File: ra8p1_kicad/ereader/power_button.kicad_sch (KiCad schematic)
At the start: 37 parts, among them Q1 DMN2056U-7, Q2 DMN2056U-7, SW1 POWER, U10 LM66100DCKR, U11 TPS3808G01DBVR, U12 74LVC1G14GW,125, U9 LTC2954ITS8-1

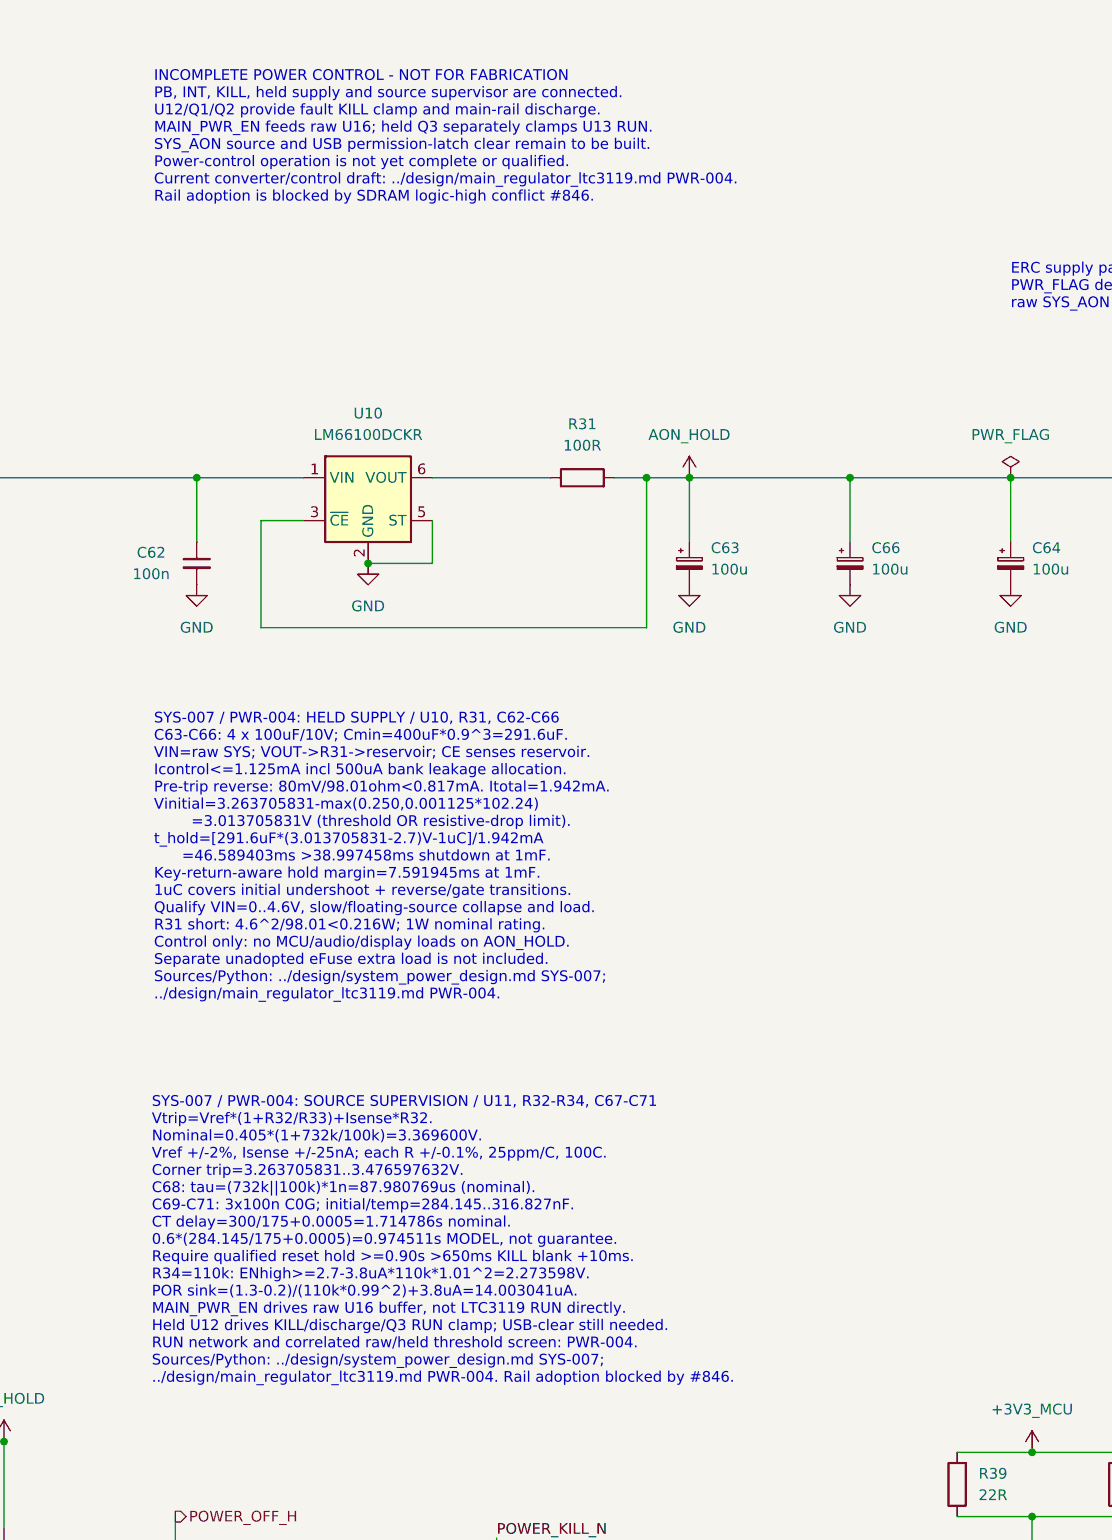
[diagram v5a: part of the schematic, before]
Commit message: Complete MCU reset checkpoint and portable engineering records
Refs #825, #826, #846. Preserve the unresolved radio release margin and unfinished schematic status; refresh full PDF and native BOM.
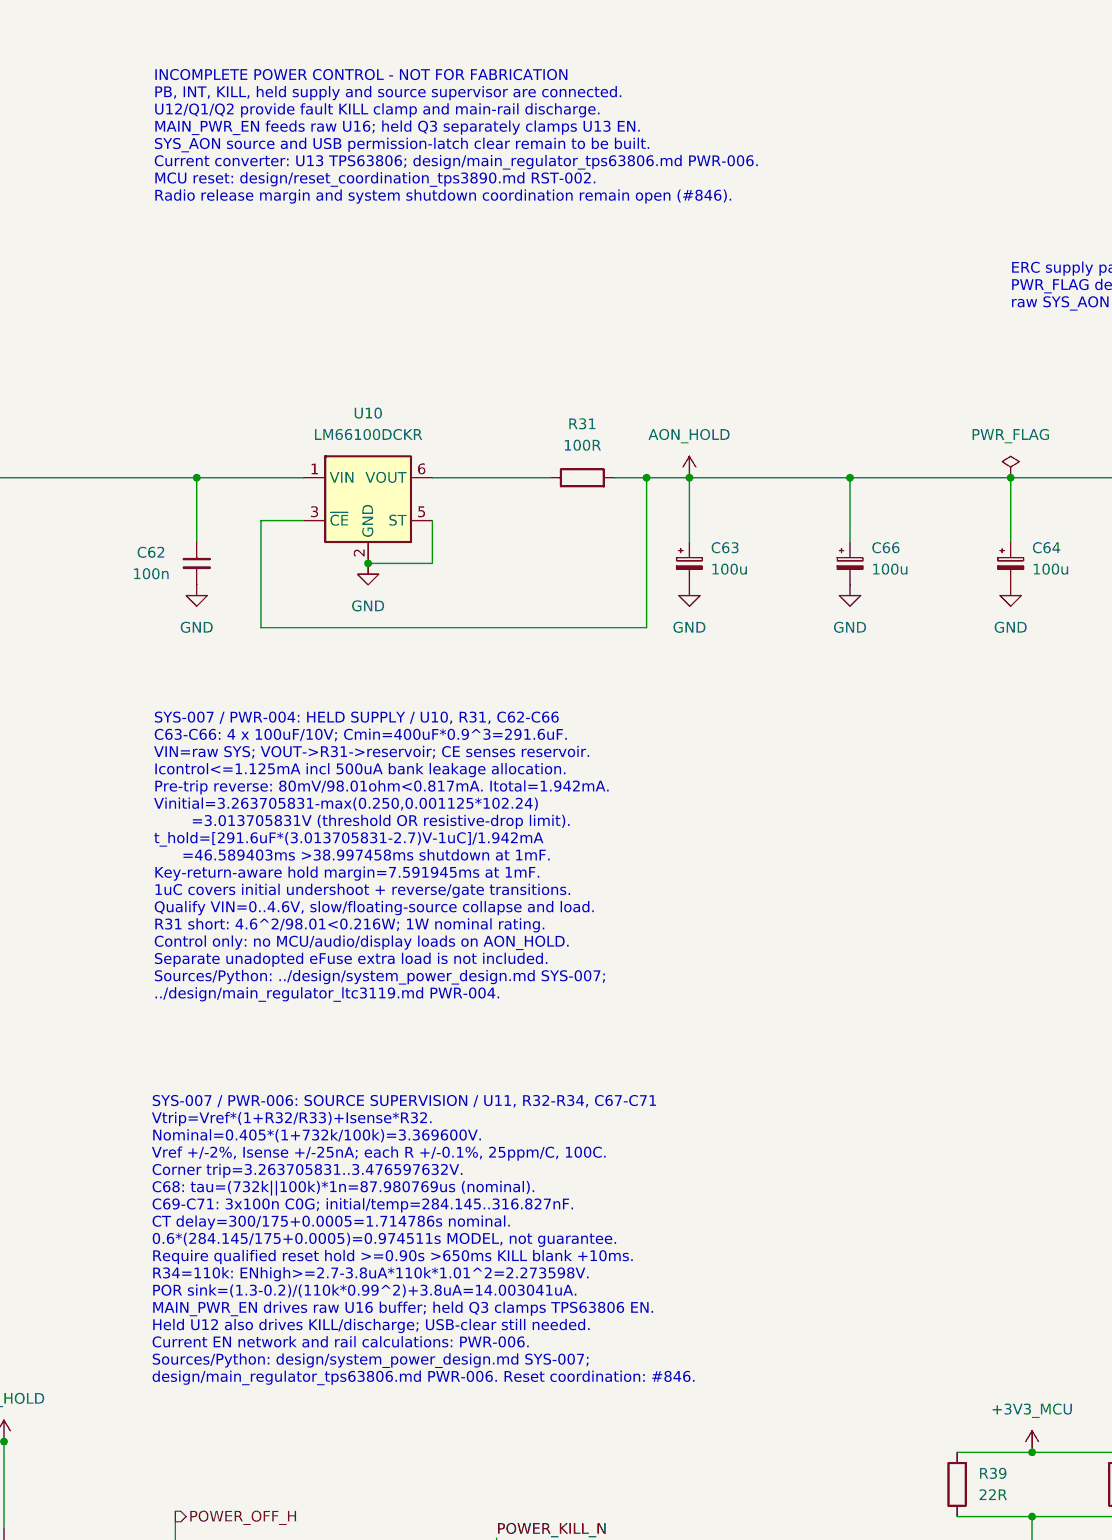
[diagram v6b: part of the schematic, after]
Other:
- note added: "INCOMPLETE POWER CONTROL - NOT FOR FABRICATION PB, INT, KILL, held supply and source supervisor are connected. U12/Q1/Q2 provide fault KILL clamp and main-rail discharge. MAIN_PWR_EN feeds raw U16; held Q3 separately clamps U13 EN. SYS_AON source and USB permission-latch clear remain to be built. Current converter: U13 TPS63806; design/main_regulator_tps63806.md PWR-006. MCU reset: design/reset_c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"
- note added: "SYS-007 / PWR-006: SOURCE SUPERVISION / U11, R32-R34, C67-C71 Vtrip=Vref*(1+R32/R33)+Isense*R32. Nominal=0.405*(1+732k/100k)=3.369600V. Vref +/-2%, Isense +/-25nA; each R +/-0.1%, 25ppm/C, 100C. Corner trip=3.263705831..3.476597632V. C68: tau=(732k||100k)*1n=87.980769us (nominal). C69-C71: 3x100n C0G; initial/temp=284.145..316.827nF. CT delay=300/175+0.0005=1.714786s nominal. 0.6*(284.145/175+0.0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"
- note removed: "INCOMPLETE POWER CONTROL - NOT FOR FABRICATION PB, INT, KILL, held supply and source supervisor are connected. U12/Q1/Q2 provide fault KILL clamp and main-rail discharge. MAIN_PWR_EN feeds raw U16; held Q3 separately clamps U13 RUN. SYS_AON source and USB permission-latch clear remain to be built. Power-control operation is not yet complete or qualified. Current converter/control draft: ../design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"
- note removed: "SYS-007 / PWR-004: SOURCE SUPERVISION / U11, R32-R34, C67-C71 Vtrip=Vref*(1+R32/R33)+Isense*R32. Nominal=0.405*(1+732k/100k)=3.369600V. Vref +/-2%, Isense +/-25nA; each R +/-0.1%, 25ppm/C, 100C. Corner trip=3.263705831..3.476597632V. C68: tau=(732k||100k)*1n=87.980769us (nominal). C69-C71: 3x100n C0G; initial/temp=284.145..316.827nF. CT delay=300/175+0.0005=1.714786s nominal. 0.6*(284.145/175+0.0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"
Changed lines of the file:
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@@
 		(rev "0.3 DRAFT")
 	)
-	(text "SYS-007 / PWR-004: SOURCE SUPERVISION / U11, R32-R34, C67-C71\nVtrip=Vref*(1+R32/R33)+Isense*R32.\nNominal=0.405*(1+732k/100k)=3.369600V.\nVref +/-2%, Isense +/-25nA; each R +/-0.1%, 25ppm/C, 100C.\nCorner trip=3.263705831..3.476597632V.\nC68: tau=(732k||100k)*1n=87.980769us (nominal).\nC69-C71: 3x100n C0G; initial/temp=284.145..316.827nF.\nCT delay=300/175+0.0005=1.714786s nominal.\n0.6*(284.145/175+0.0005)=0.974511s MODEL, not guarantee.\nRequire qualified reset hold >=0.90s >650ms KILL blank +10ms.\nR34=110k: ENhigh>=2.7-3.8uA*110k*1.01^2=2.273598V.\nPOR sink=(1.3-0.2)/(110k*0.99^2)+3.8uA=14.003041uA.\nMAIN_PWR_EN drives raw U16 buffer, not LTC3119 RUN directly.\nHeld U12 drives KILL/discharge/Q3 RUN clamp; USB-clear still needed.\nRUN network and correlated raw/held threshold screen: PWR-004.\nSources/Python: ../design/system_power_design.md SYS-007;\n../design/main_regulator_ltc3119.md PWR-004. Rail adoption blocked by #846."
+	(text "SYS-007 / PWR-006: SOURCE SUPERVISION / U11, R32-R34, C67-C71\nVtrip=Vref*(1+R32/R33)+Isense*R32.\nNominal=0.405*(1+732k/100k)=3.369600V.\nVref +/-2%, Isense +/-25nA; each R +/-0.1%, 25ppm/C, 100C.\nCorner trip=3.263705831..3.476597632V.\nC68: tau=(732k||100k)*1n=87.980769us (nominal).\nC69-C71: 3x100n C0G; initial/temp=284.145..316.827nF.\nCT delay=300/175+0.0005=1.714786s nominal.\n0.6*(284.145/175+0.0005)=0.974511s MODEL, not guarantee.\nRequire qualified reset hold >=0.90s >650ms KILL blank +10ms.\nR34=110k: ENhigh>=2.7-3.8uA*110k*1.01^2=2.273598V.\nPOR sink=(1.3-0.2)/(110k*0.99^2)+3.8uA=14.003041uA.\nMAIN_PWR_EN drives raw U16 buffer; held Q3 clamps TPS63806 EN.\nHeld U12 also drives KILL/discharge; USB-clear still needed.\nCurrent EN network and rail calculations: PWR-006.\nSources/Python: design/system_power_design.md SYS-007;\ndesign/main_regulator_tps63806.md PWR-006. Reset coordination: #846."
 		(exclude_from_sim no)
 		(at 228.346 172.466 0)
@@
 			)
 			(justify left top)
-			(href "https://github.com/bsikar/ra8-firmware/blob/design/ereader-circuit/ra8p1_kicad/design/main_regulator_ltc3119.md")
+			(href "https://github.com/bsikar/ra8-firmware/blob/design/ereader-circuit/ra8p1_kicad/design/main_regulator_tps63806.md")
 		)
 	)
@@
 		)
 	)
-	(text "INCOMPLETE POWER CONTROL - NOT FOR FABRICATION\nPB, INT, KILL, held supply and source supervisor are connected.\nU12/Q1/Q2 provide fault KILL clamp and main-rail discharge.\nMAIN_PWR_EN feeds raw U16; held Q3 separately clamps U13 RUN.\nSYS_AON source and USB permission-latch clear remain to be built.\nPower-control operation is not yet complete or qualified.\nCurrent converter/control draft: ../design/main_regulator_ltc3119.md PWR-004.\nRail adoption is blocked by SDRAM logic-high conflict #846."
+	(text "INCOMPLETE POWER CONTROL - NOT FOR FABRICATION\nPB, INT, KILL, held supply and source supervisor are connected.\nU12/Q1/Q2 provide fault KILL clamp and main-rail discharge.\nMAIN_PWR_EN feeds raw U16; held Q3 separately clamps U13 EN.\nSYS_AON source and USB permission-latch clear remain to be built.\nCurrent converter: U13 TPS63806; design/main_regulator_tps63806.md PWR-006.\nMCU reset: design/reset_coordination_tps3890.md RST-002.\nRadio release margin and system shutdown coordination remain open (#846)."
 		(exclude_from_sim no)
 		(at 228.6 50.8 0)
@@
 			)
 			(justify left top)
-			(href "https://github.com/bsikar/ra8-firmware/blob/design/ereader-circuit/ra8p1_kicad/design/main_regulator_ltc3119.md")
+			(href "https://github.com/bsikar/ra8-firmware/blob/design/ereader-circuit/ra8p1_kicad/design/main_regulator_tps63806.md")
 		)
 	)

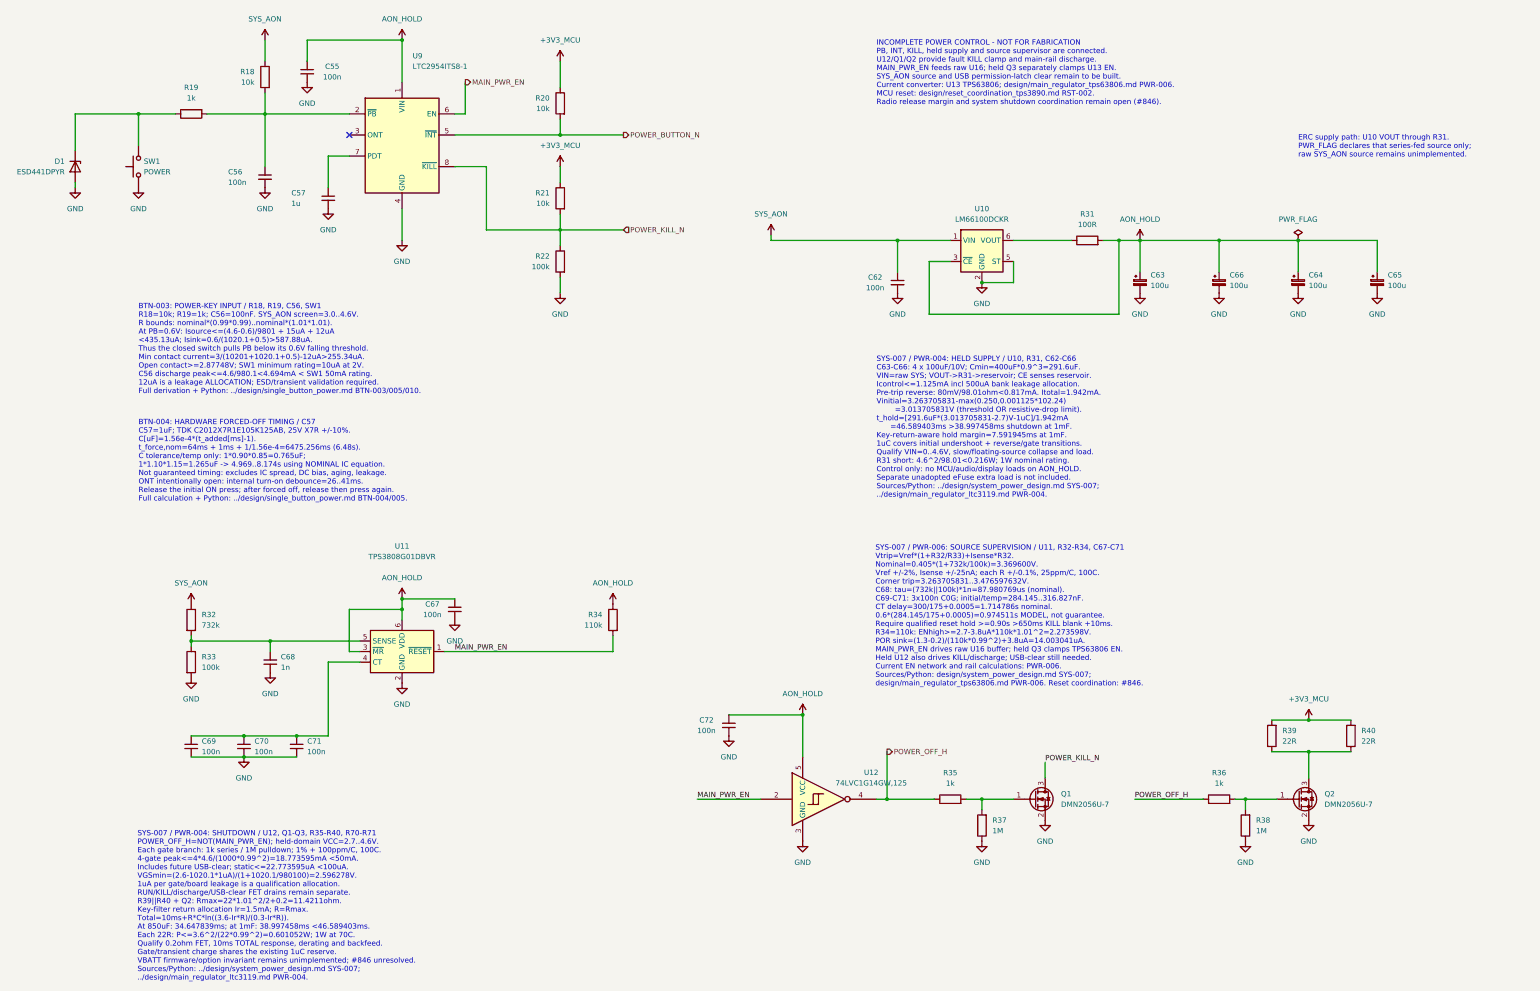
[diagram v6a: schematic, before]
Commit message: wip(hardware): preserve schematic cleanup and CEU host ports
Checkpoint cosmetic cleanup across the schematic hierarchy and eleven parallel-camera host ports. Refresh the complete 13-page PDF. All 334 existing net partitions and 271 component records match the prior CEU checkpoint; all 128 ERC identities remain unchanged. Electrical design is incomplete; this is a WIP checkpoint for #821 and #841.
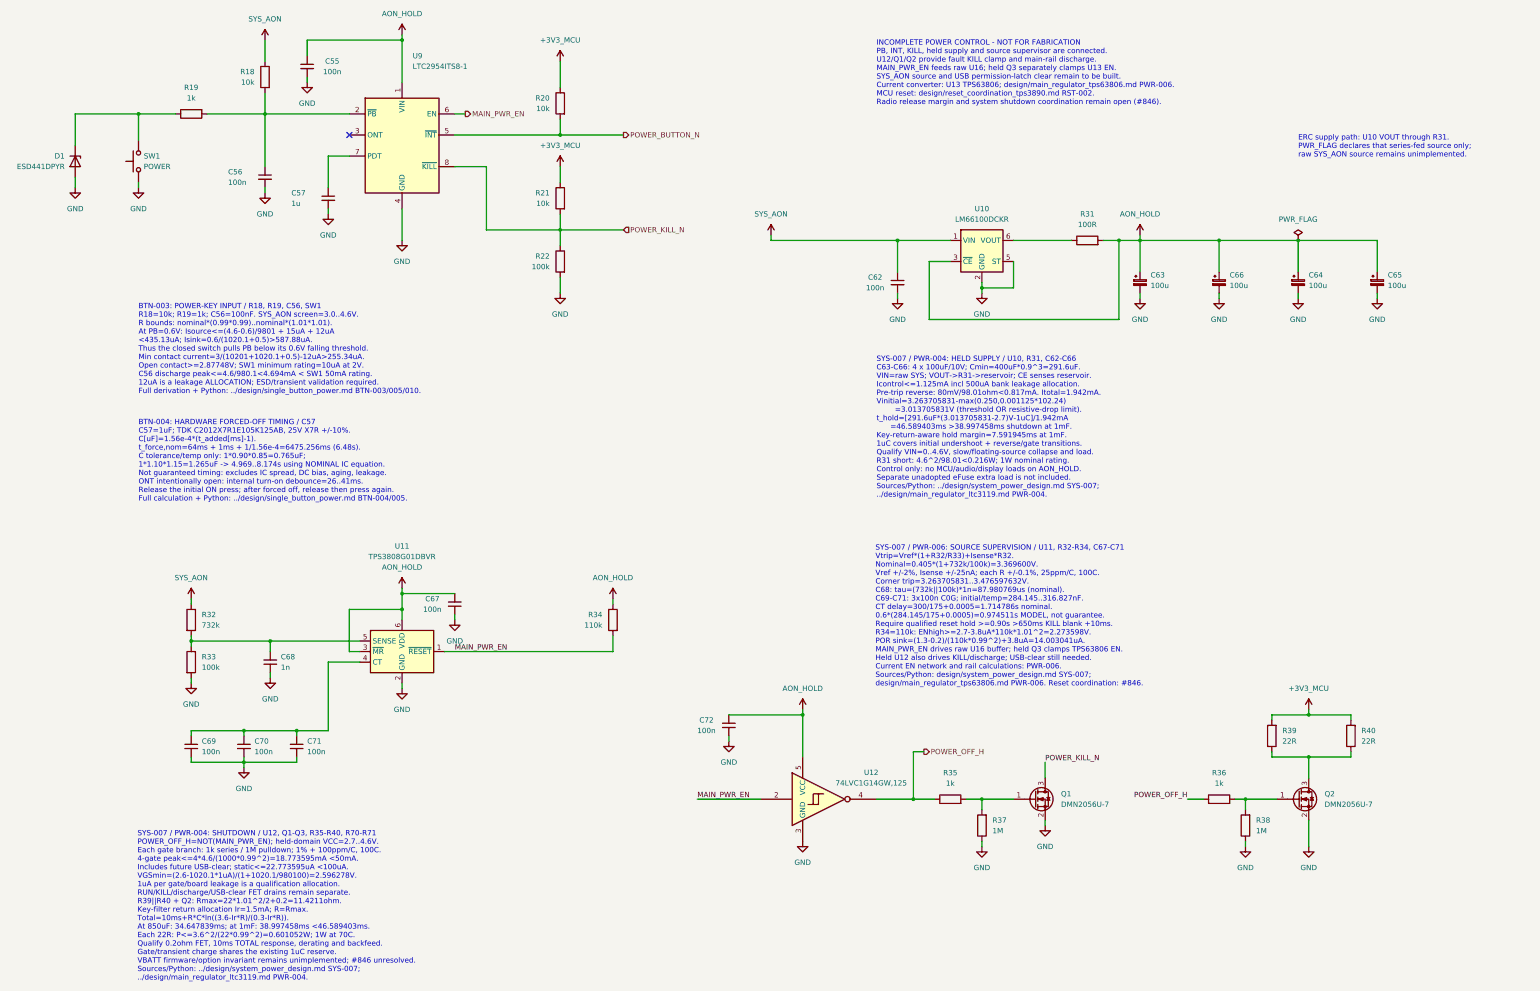
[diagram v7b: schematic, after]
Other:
- moved on the sheet: C55, C67, D1, SW1
